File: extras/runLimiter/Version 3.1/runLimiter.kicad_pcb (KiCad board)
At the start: 2 copper layers, 70 x 50 mm, 19 parts, among them J1 5-20 Volts, J2 Vout, J3 Dry Contacts, K1 Relay, Q1 2N3904, Q2 2SD2023, U1 MCP1700-330, U2 ESP8266-01s

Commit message: Updated version number on silkscreen
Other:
- board text added: "Runtime Limiter David E. Powell Ver. 3.1 08/16/2023"
- board text removed: "Runtime Limiter David E. Powell Ver. 3.0 08/16/2023"
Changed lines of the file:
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@@
     (effects (font (size 1.5 1.5) (thickness 0.3)))
   )
-  (gr_text "Runtime Limiter\nDavid E. Powell\nVer. 3.0\n08/16/2023" (at 49.5 5.5) (layer "F.SilkS")
+  (gr_text "Runtime Limiter\nDavid E. Powell\nVer. 3.1\n08/16/2023" (at 49.5 5.5) (layer "F.SilkS")
     (effects (font (size 1.5 1.5) (thickness 0.2)))
   )

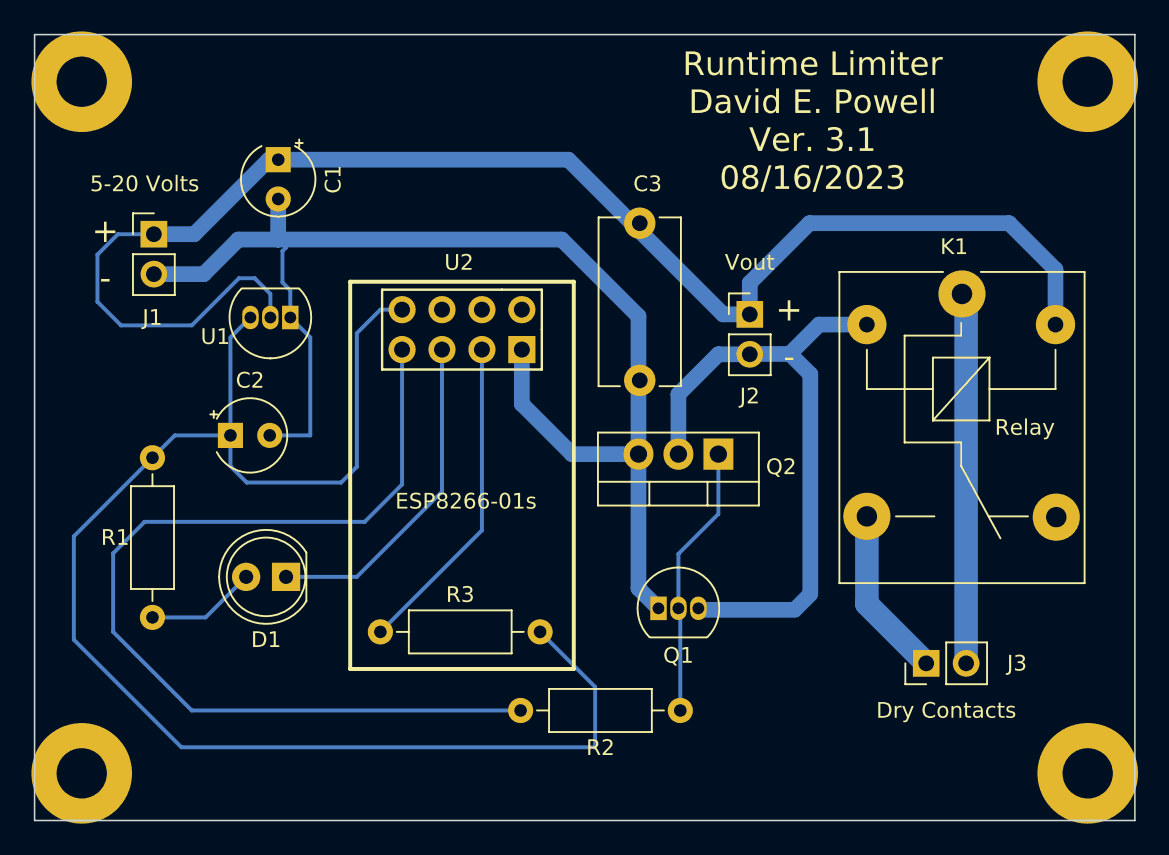
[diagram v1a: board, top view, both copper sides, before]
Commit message: Changes to board and schematic
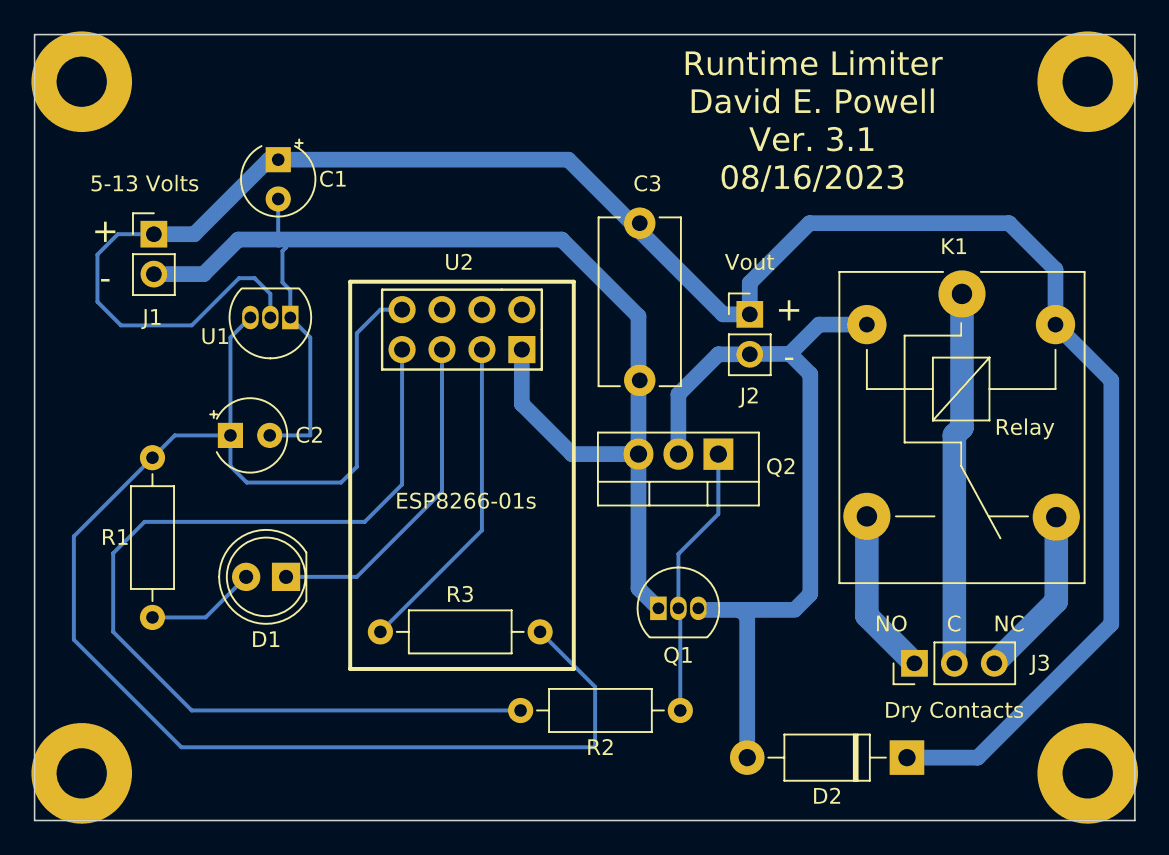
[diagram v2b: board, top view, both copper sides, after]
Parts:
- added D2: 1N4003, Diode_THT:D_DO-41_SOD81_P10.16mm_Horizontal, F.Cu at (55.5, 46.0)
- J1: value 5-20 Volts -> 5-13 Volts
- J3: footprint Connector_PinHeader_2.54mm:PinHeader_1x02_P2.54mm_Vertical -> Connector_PinHeader_2.54mm:PinHeader_1x03_P2.54mm_Vertical
- U1: value MCP1700-330 -> MCP1702T-3302E/TO
- moved J3 0.75 mm to (56.0, 40.0)
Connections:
- K1 pad 4: unconnected-(K1-Pad4) -> Net-(J3-Pad3)
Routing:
- net /Control Power: track 94.2 -> 131.3 mm
- net Net-(J3-Pad3): track 0.00 -> 10.9 mm
- net /Control Ground: track 40.8 -> 50.4 mm
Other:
- board text added: "C"
- board text added: "NC"
- board text added: "NO"
